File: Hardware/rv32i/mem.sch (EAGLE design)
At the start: 27 parts, among them IC1 IS61C5128AS-25QLI, IC10 SN74HC138PWR, IC2 IS61C5128AS-25QLI, IC3 IS61C5128AS-25QLI, IC4 IS61C5128AS-25QLI, IC5 IS61C5128AS-25QLI, IC6 IS61C5128AS-25QLI, IC7 IS61C5128AS-25QLI, IC8 IS61C5128AS-25QLI, IC9 SN74HC138PWR

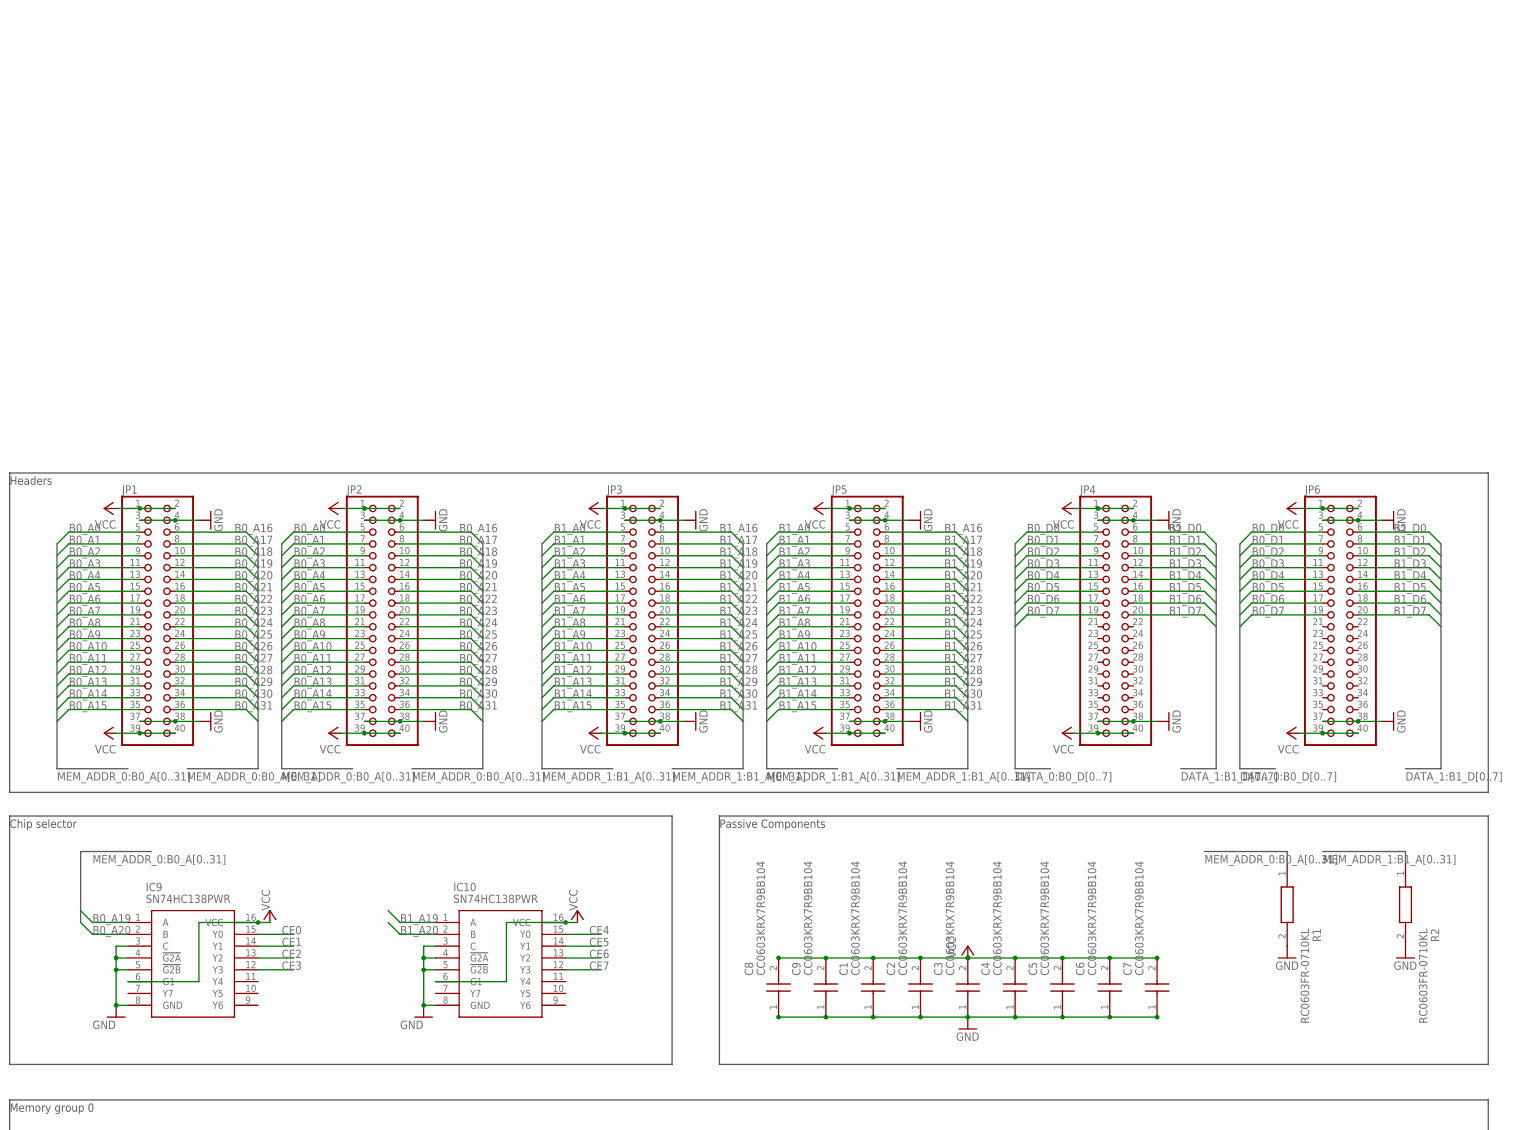
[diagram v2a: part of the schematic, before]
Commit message: Memory pcb layout
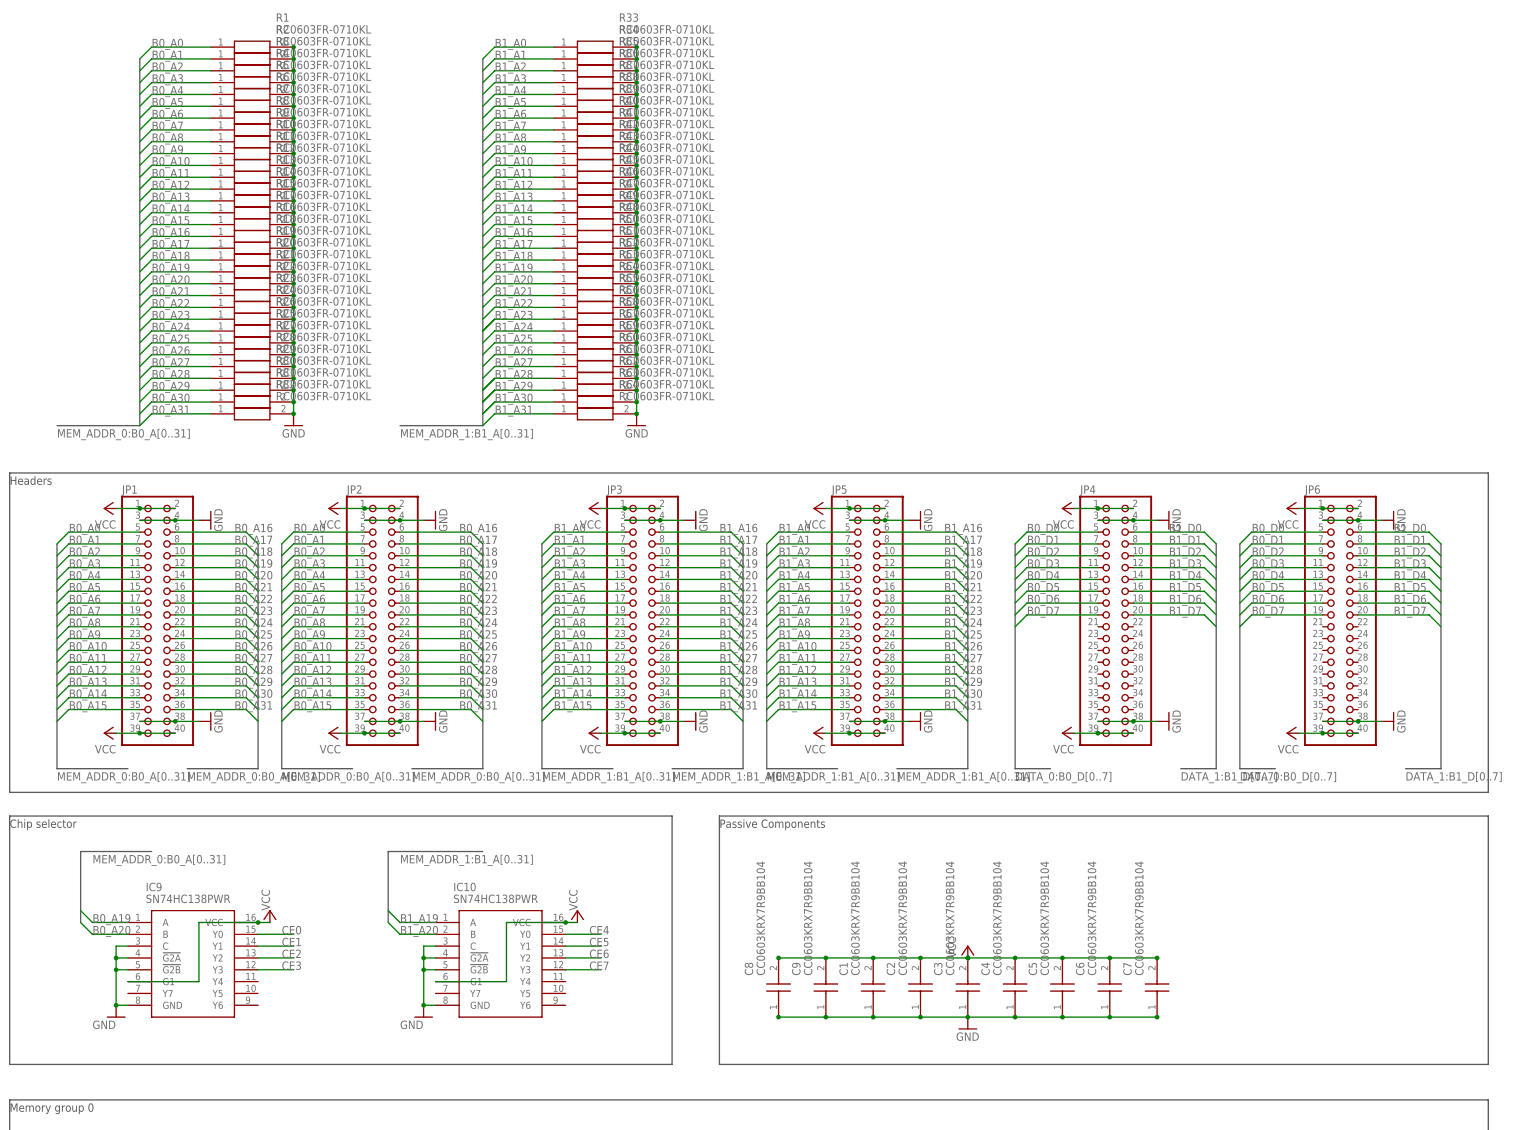
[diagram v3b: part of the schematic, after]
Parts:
- added R10, R11, R12, R13, R14, R15, R16, R17, R18, R19, R20, R21, R22, R23, R24, R25, R26, R27, R28, R29, R3, R30, R31, R32, R33, R34, R35, R36, R37, R38, R39, R4, R40, R41, R42, R43, R44, R45, R46, R47, R48, R49, R5, R50, R51, R52, R53, R54, R55, R56, R57, R58, R59, R6, R60, R61, R62, R63, R64, R7, R8, R9: RC0603FR-0710KL, RC0603FR-0710KL:RC0603FR-0710KL
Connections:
- net B0_A0: now also R1.1
- net B0_A1: now also R2.1
- net B0_A10: now also R11.1
- net B0_A11: now also R12.1
- net B0_A12: now also R13.1
- net B0_A13: now also R14.1
- net B0_A14: now also R15.1
- net B0_A15: now also R17.1
- net B0_A16: now also R16.1
- net B0_A17: now also R18.1
- net B0_A18: now also R19.1
- net B0_A19: now also R20.1
- net B0_A2: now also R3.1
- net B0_A20: now also R21.1
- net B0_A21: now also R22.1
- net B0_A22: now also R23.1
- net B0_A23: now also R24.1
- net B0_A24: now also R26.1
- net B0_A25: now also R25.1
- net B0_A26: now also R27.1
- net B0_A27: now also R28.1
- net B0_A28: now also R29.1
- net B0_A29: now also R30.1
- net B0_A3: now also R4.1
- net B0_A30: now also R31.1
- net B0_A31: now also R32.1
- net B0_A4: now also R5.1
- net B0_A5: now also R6.1
- net B0_A6: now also R7.1
- net B0_A7: now also R8.1
- net B0_A8: now also R9.1
- net B0_A9: now also R10.1
- net B1_A0: now also R33.1
- net B1_A1: now also R34.1
- net B1_A10: now also R43.1
- net B1_A11: now also R44.1
- net B1_A12: now also R45.1
- net B1_A13: now also R46.1
- net B1_A14: now also R47.1
- net B1_A15: now also R49.1
- net B1_A16: now also R48.1
- net B1_A17: now also R50.1
- net B1_A18: now also R51.1
- net B1_A19: now also R52.1
- net B1_A2: now also R35.1
- net B1_A20: now also R53.1
- net B1_A21: now also R54.1
- net B1_A22: now also R55.1
- net B1_A23: now also R56.1
- net B1_A24: now also R58.1
- net B1_A25: now also R57.1
- net B1_A26: now also R59.1
- net B1_A27: now also R60.1
- net B1_A28: now also R61.1
- net B1_A29: now also R62.1
- net B1_A3: now also R36.1
- net B1_A30: now also R63.1
- net B1_A31: now also R64.1
- net B1_A4: now also R37.1
- net B1_A5: now also R38.1
- net B1_A6: now also R39.1
- net B1_A7: now also R40.1
- net B1_A8: now also R41.1
- net B1_A9: now also R42.1
- net GND: now also R10.2, R11.2, R12.2, R13.2, R14.2, R15.2, R16.2, R17.2, R18.2, R19.2, R20.2, R21.2, R22.2, R23.2, R24.2, R25.2, R26.2, R27.2, R28.2, R29.2, R3.2, R30.2, R31.2, R32.2, R33.2, R34.2, R35.2, R36.2, R37.2, R38.2, R39.2, R4.2, R40.2, R41.2, R42.2, R43.2, R44.2, R45.2, R46.2, R47.2, R48.2, R49.2, R5.2, R50.2, R51.2, R52.2, R53.2, R54.2, R55.2, R56.2, R57.2, R58.2, R59.2, R6.2, R60.2, R61.2, R62.2, R63.2, R64.2, R7.2, R8.2, R9.2
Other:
- moved on the sheet: R1, R2

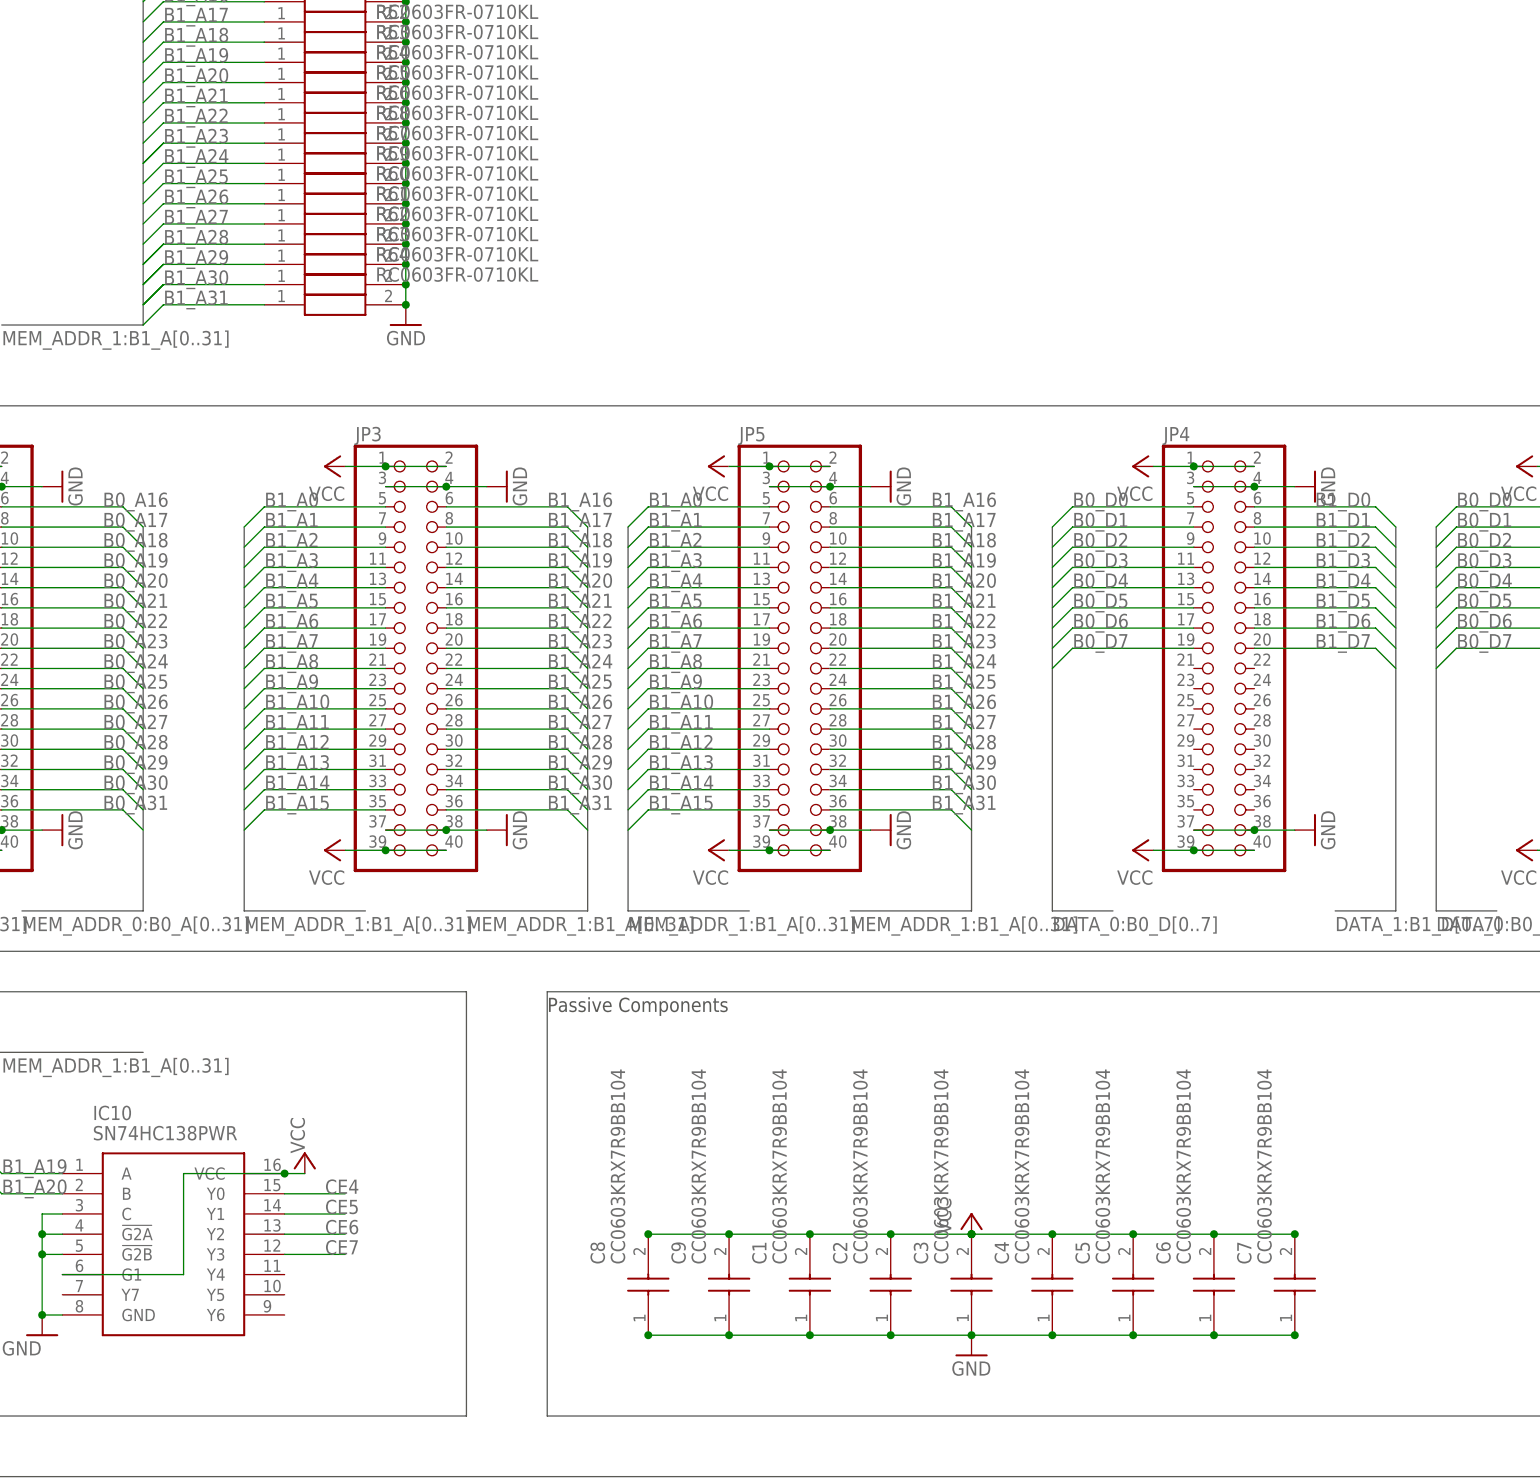
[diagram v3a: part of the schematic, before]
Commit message: Update memory schematic & parts
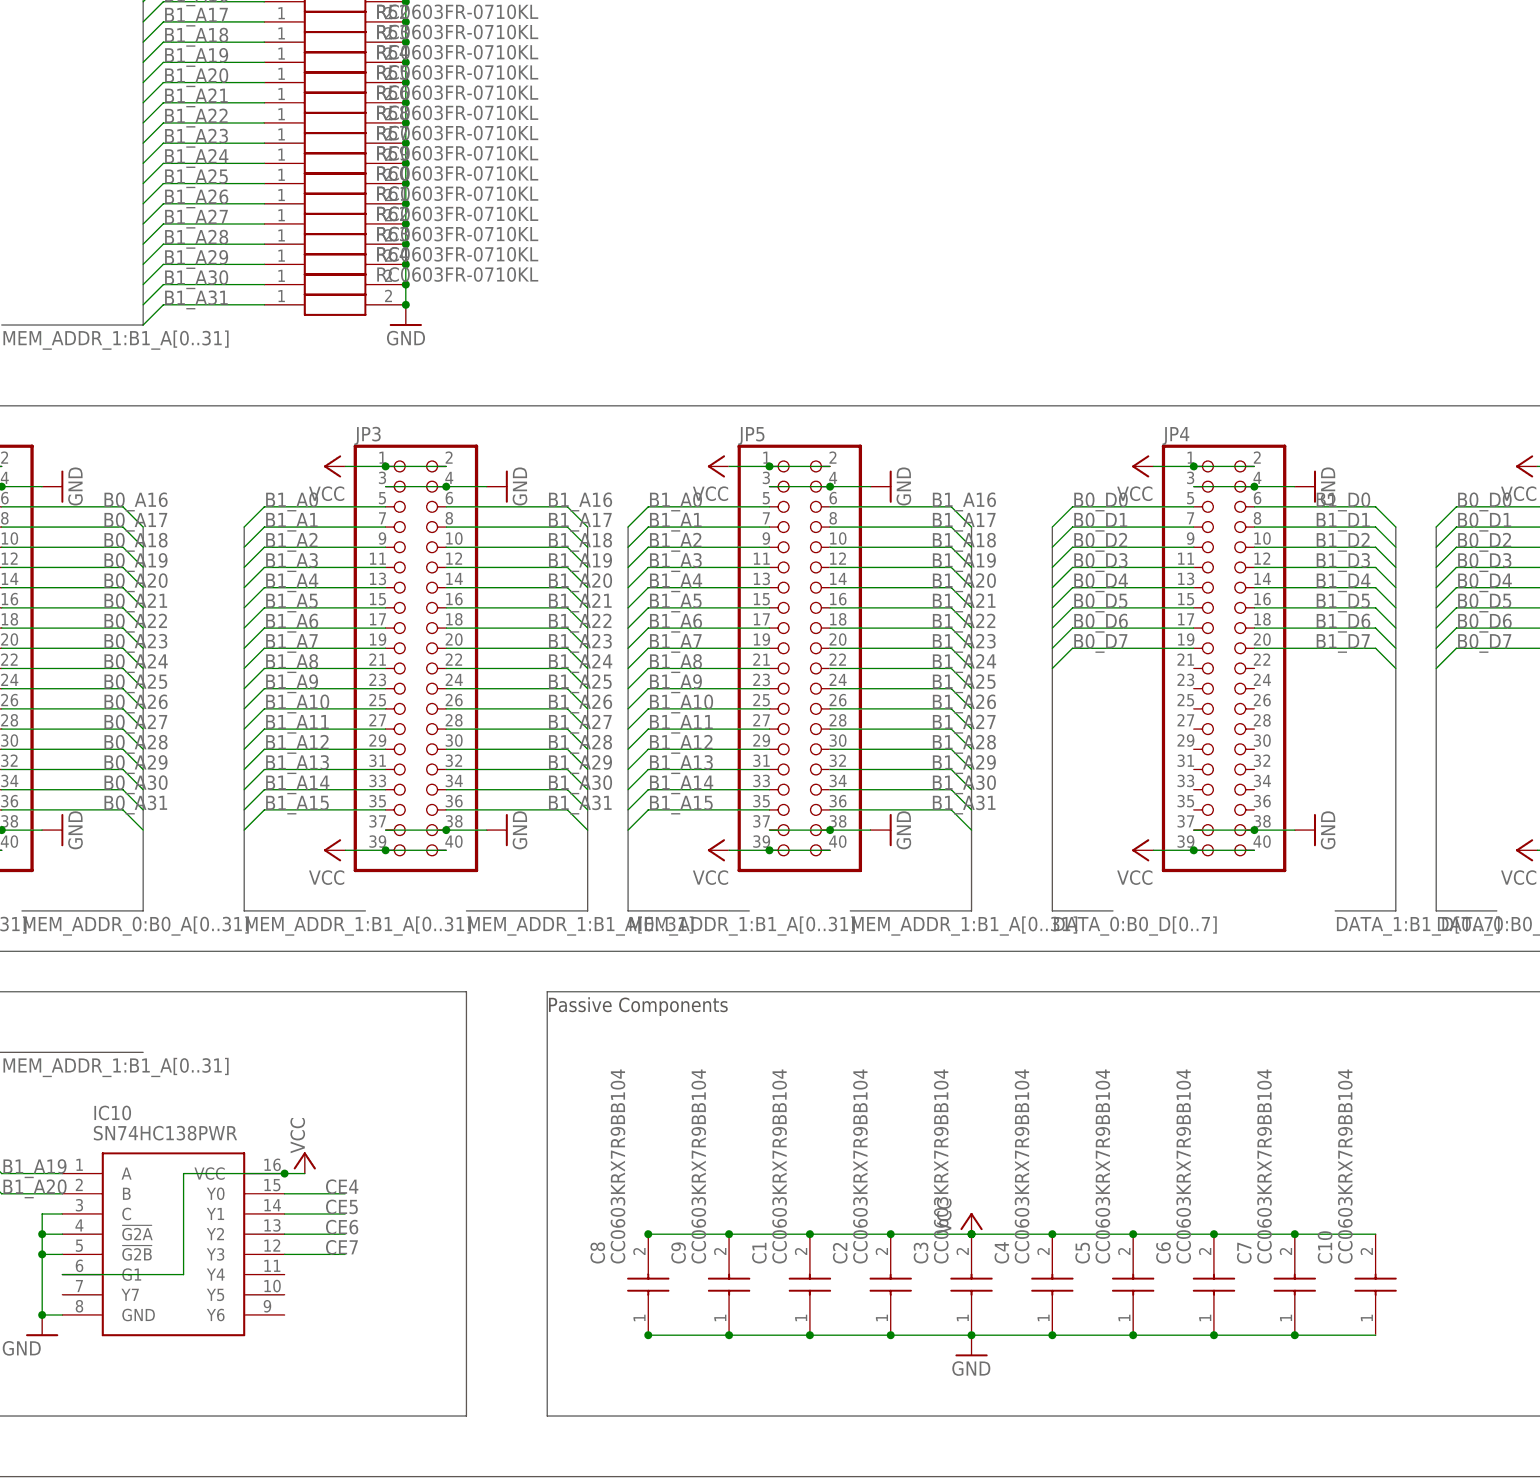
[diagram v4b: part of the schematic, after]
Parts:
- added C10: CC0603KRX7R9BB104, CC0603KRX7R9BB104:CC0603KRX7R9BB104
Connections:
- net GND: now also C10.1
- net VCC: now also C10.2
